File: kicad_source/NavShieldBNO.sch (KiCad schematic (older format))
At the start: 48 parts, among them CN1 ARDUINO_MKR, CN2 CONN_01X04, CN3 CONN_01X04, U1 BNO085, U2 BMP388, U3 BMP280, U4 BME280, Y1 DNI

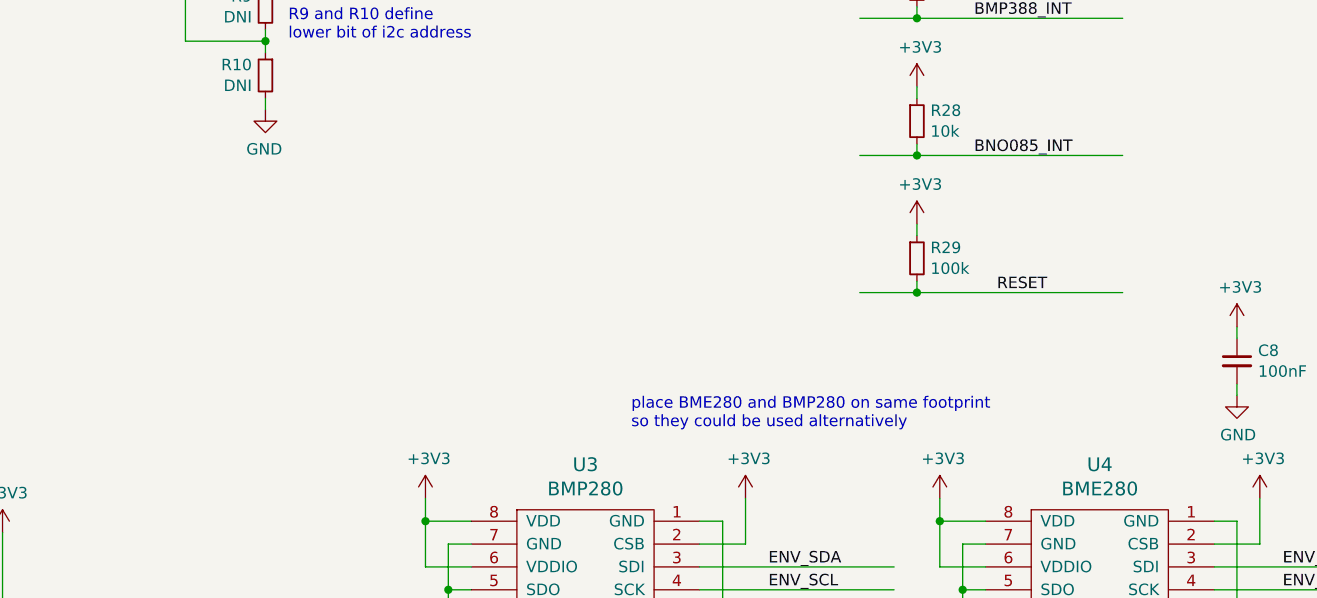
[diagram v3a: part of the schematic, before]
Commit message: added Vishay VCNL4040
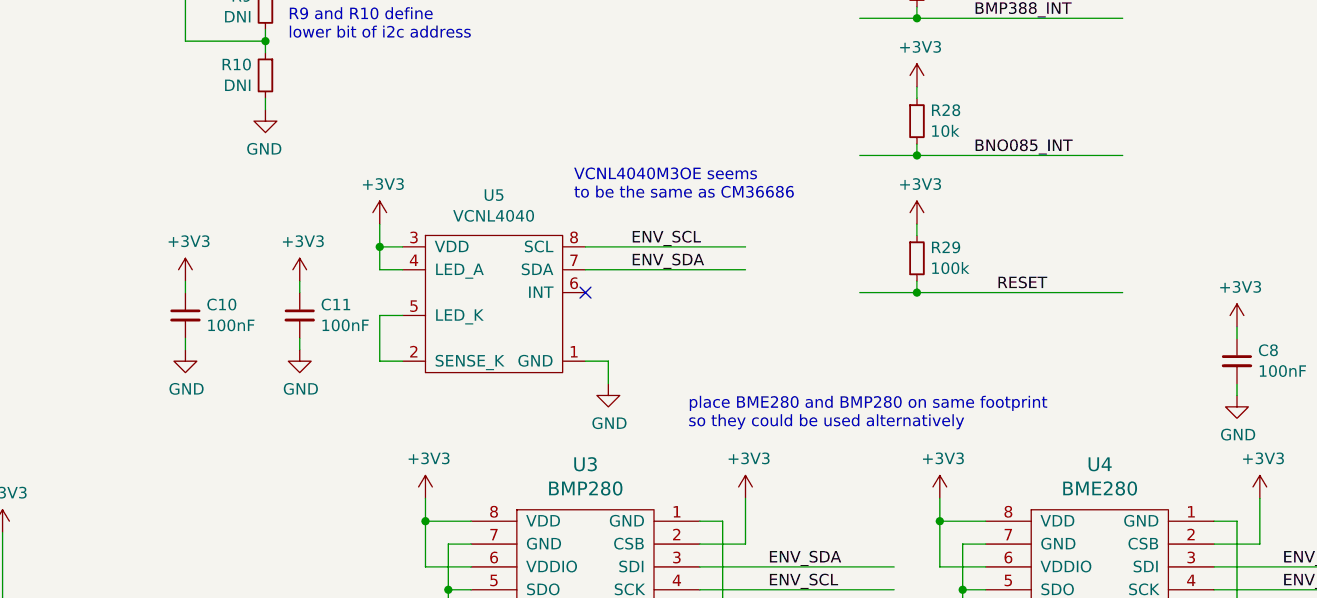
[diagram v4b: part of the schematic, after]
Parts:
- added C10, C11: 100nF, capacitors:C_0603, symbol devices:C_0603
- added U5: VCNL4040, IC_sensor:VCNL4040, symbol IC_sensor:VCNL4040
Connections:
- wire segments 210 -> 225
- no-connect marks 12 -> 13
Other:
- note added: "VCNL4040M3OE seems \nto be the same as CM36686"
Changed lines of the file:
@@
 Wire Wire Line
 	10850 5000 10850 5050
-Text Notes 7700 5450 0    50   ~ 0
+Text Notes 7950 5450 0    50   ~ 0
 place BME280 and BMP280 on same footprint\nso they could be used alternatively
+Text Notes 7450 4450 0    50   ~ 0
+VCNL4040M3OE seems \nto be the same as CM36686
+$Comp
+L IC_sensor:VCNL4040 U5
+U 1 1 5F712BB0
+P 7100 4900
+F 0 "U5" H 7100 5375 50  0000 C CNN
+F 1 "VCNL4040" H 7100 5284 50  0000 C CNN
+F 2 "IC_sensor:VCNL4040" H 7150 4750 50  0001 C CNN
+F 3 "" H 7150 4750 50  0001 C CNN
+	1    7100 4900
+	1    0    0    -1
+$EndComp
+$Comp
+L devices:C_0603 C10
+U 1 1 5F7145FC
+P 5750 4950
+F 0 "C10" H 5842 4996 50  0000 L CNN
+F 1 "100nF" H 5842 4905 50  0000 L CNN
+F 2 "capacitors:C_0603" H 5750 4800 50  0001 C CNN
+F 3 "" H 5750 4950 50  0000 C CNN
+	1    5750 4950
+	1    0    0    -1
+$EndComp
+$Comp
+L power-supply:GND #PWR050
+U 1 1 5F714606
+P 5750 5100
+F 0 "#PWR050" H 5750 4850 50  0001 C CNN
+F 1 "GND" H 5755 4927 50  0000 C CNN
+F 2 "" H 5750 5100 50  0000 C CNN
+F 3 "" H 5750 5100 50  0000 C CNN
+	1    5750 5100
+	1    0    0    -1
+$EndComp
+$Comp
+L power-supply:+3V3 #PWR049
+U 1 1 5F714610
+P 5750 4800
+F 0 "#PWR049" H 5750 4650 50  0001 C CNN
+F 1 "+3V3" H 5765 4973 50  0000 C CNN
+F 2 "" H 5750 4800 50  0000 C CNN
+F 3 "" H 5750 4800 50  0000 C CNN
+	1    5750 4800
+	1    0    0    -1
+$EndComp
+Wire Wire Line
+	5750 5050 5750 5100
+Wire Wire Line
+	5750 4800 5750 4850
+$Comp
+L devices:C_0603 C11
+U 1 1 5F71461C
+P 6250 4950
+F 0 "C11" H 6342 4996 50  0000 L CNN
+F 1 "100nF" H 6342 4905 50  0000 L CNN
+F 2 "capacitors:C_0603" H 6250 4800 50  0001 C CNN
+F 3 "" H 6250 4950 50  0000 C CNN
+	1    6250 4950
+	1    0    0    -1
+$EndComp
+$Comp
+L power-supply:GND #PWR052
+U 1 1 5F714626
+P 6250 5100
+F 0 "#PWR052" H 6250 4850 50  0001 C CNN
+F 1 "GND" H 6255 4927 50  0000 C CNN
+F 2 "" H 6250 5100 50  0000 C CNN
+F 3 "" H 6250 5100 50  0000 C CNN
+	1    6250 5100
+	1    0    0    -1
+$EndComp
+$Comp
+L power-supply:+3V3 #PWR051
+U 1 1 5F714630
+P 6250 4800
+F 0 "#PWR051" H 6250 4650 50  0001 C CNN
+F 1 "+3V3" H 6265 4973 50  0000 C CNN
+F 2 "" H 6250 4800 50  0000 C CNN
+F 3 "" H 6250 4800 50  0000 C CNN
+	1    6250 4800
+	1    0    0    -1
+$EndComp
+Wire Wire Line
+	6250 5050 6250 5100
+Wire Wire Line
+	6250 4800 6250 4850
+$Comp
+L power-supply:+3V3 #PWR053
+U 1 1 5F722D98
+P 6600 4550
+F 0 "#PWR053" H 6600 4400 50  0001 C CNN
+F 1 "+3V3" H 6615 4723 50  0000 C CNN
+F 2 "" H 6600 4550 50  0000 C CNN
+F 3 "" H 6600 4550 50  0000 C CNN
+	1    6600 4550
+	1    0    0    -1
+$EndComp
+$Comp
+L power-supply:GND #PWR054
+U 1 1 5F723279
+P 7600 5250
+F 0 "#PWR054" H 7600 5000 50  0001 C CNN
+F 1 "GND" H 7605 5077 50  0000 C CNN
+F 2 "" H 7600 5250 50  0000 C CNN
+F 3 "" H 7600 5250 50  0000 C CNN
+	1    7600 5250
+	1    0    0    -1
+$EndComp
+Wire Wire Line
+	8200 4650 7500 4650
+Wire Wire Line
+	8200 4750 7500 4750
+Wire Wire Line
+	7500 5150 7600 5150
+Wire Wire Line
+	7600 5150 7600 5250
+Wire Wire Line
+	6700 5150 6600 5150
+Wire Wire Line
+	6600 5150 6600 4950
+Wire Wire Line
+	6600 4950 6700 4950
+Wire Wire Line
+	6700 4750 6600 4750
+Wire Wire Line
+	6600 4750 6600 4650
+Wire Wire Line
+	6700 4650 6600 4650
+Connection ~ 6600 4650
+Wire Wire Line
+	6600 4650 6600 4550
+Text Label 7700 4750 0    50   ~ 0
+ENV_SDA
+Text Label 7700 4650 0    50   ~ 0
+ENV_SCL
+NoConn ~ 7500 4850
 $EndSCHEMATC

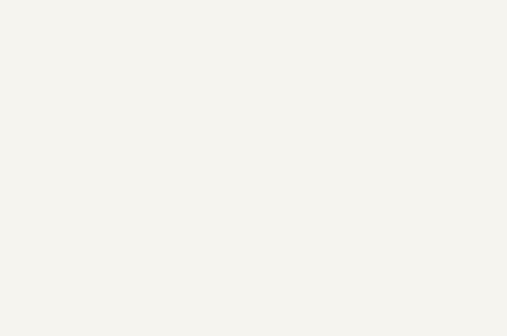
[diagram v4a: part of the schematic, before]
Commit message: added logo, updated images and pdf
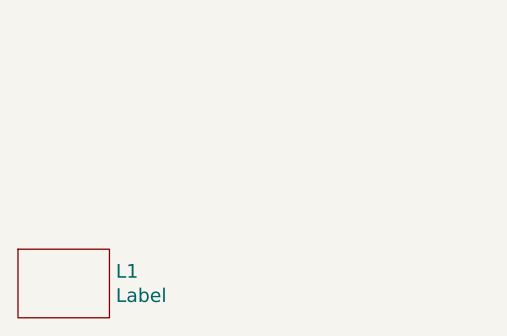
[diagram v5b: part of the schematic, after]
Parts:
- added L1: Label, labels:generationmake_small_solder, symbol devices:Label
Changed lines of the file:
@@
 Sheet 1 1
 Title "NavShieldBNO"
-Date "2020-09-25"
-Rev "dev_0.1"
+Date "2020-09-27"
+Rev "0.1"
 Comp "generationmake"
 Comment1 ""
@@
 ENV_SCL
 NoConn ~ 7500 4850
+$Comp
+L devices:Label L1
+U 1 1 5F79EEB6
+P 700 7600
+F 0 "L1" H 928 7653 60  0000 L CNN
+F 1 "Label" H 928 7547 60  0000 L CNN
+F 2 "labels:generationmake_small_solder" H 600 7700 60  0001 C CNN
+F 3 "" H 700 7600 60  0000 C CNN
+	1    700  7600
+	1    0    0    -1
+$EndComp
 $EndSCHEMATC

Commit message: updated layout, made DRC, updated silk screen
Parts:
- added L2: Label, labels:generationmake_logo, symbol devices:Label
- added W1, W2, W3, W4, W5, W6, W7, W8: TEST_1P, wire_pads:SolderWirePad_single_1mmSMD, symbol mechanical-connectors:TEST_1P
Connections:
- net labels added: INT
- wire segments 225 -> 231
- no-connect marks 13 -> 12
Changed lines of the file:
@@
 Text Label 7700 4650 0    50   ~ 0
 ENV_SCL
-NoConn ~ 7500 4850
 $Comp
 L devices:Label L1
@@
 	1    0    0    -1
 $EndComp
+$Comp
+L mechanical-connectors:TEST_1P W3
+U 1 1 5F71EF96
+P 5800 6700
+F 0 "W3" V 5750 6650 50  0000 L CNN
+F 1 "TEST_1P" V 5845 6888 50  0000 L CNN
+F 2 "wire_pads:SolderWirePad_single_1mmSMD" H 6000 6700 50  0001 C CNN
+F 3 "" H 6000 6700 50  0000 C CNN
+	1    5800 6700
+	0    1    1    0
+$EndComp
+$Comp
+L mechanical-connectors:TEST_1P W4
+U 1 1 5F71FCBA
+P 5800 6800
+F 0 "W4" V 5750 6750 50  0000 L CNN
+F 1 "TEST_1P" V 5845 6988 50  0000 L CNN
+F 2 "wire_pads:SolderWirePad_single_1mmSMD" H 6000 6800 50  0001 C CNN
+F 3 "" H 6000 6800 50  0000 C CNN
+	1    5800 6800
+	0    1    1    0
+$EndComp
+$Comp
+L mechanical-connectors:TEST_1P W5
+U 1 1 5F71FE99
+P 5800 6900
+F 0 "W5" V 5750 6850 50  0000 L CNN
+F 1 "TEST_1P" V 5845 7088 50  0000 L CNN
+F 2 "wire_pads:SolderWirePad_single_1mmSMD" H 6000 6900 50  0001 C CNN
+F 3 "" H 6000 6900 50  0000 C CNN
+	1    5800 6900
+	0    1    1    0
+$EndComp
+$Comp
+L mechanical-connectors:TEST_1P W6
+U 1 1 5F720010
+P 5800 7000
+F 0 "W6" V 5750 6950 50  0000 L CNN
+F 1 "TEST_1P" V 5845 7188 50  0000 L CNN
+F 2 "wire_pads:SolderWirePad_single_1mmSMD" H 6000 7000 50  0001 C CNN
+F 3 "" H 6000 7000 50  0000 C CNN
+	1    5800 7000
+	0    1    1    0
+$EndComp
+$Comp
+L mechanical-connectors:TEST_1P W7
+U 1 1 5F72016B
+P 5800 7100
+F 0 "W7" V 5750 7050 50  0000 L CNN
+F 1 "TEST_1P" V 5845 7288 50  0000 L CNN
+F 2 "wire_pads:SolderWirePad_single_1mmSMD" H 6000 7100 50  0001 C CNN
+F 3 "" H 6000 7100 50  0000 C CNN
+	1    5800 7100
+	0    1    1    0
+$EndComp
+$Comp
+L mechanical-connectors:TEST_1P W1
+U 1 1 5F72032F
+P 2000 3450
+F 0 "W1" V 1954 3638 50  0000 L CNN
+F 1 "TEST_1P" V 2045 3638 50  0000 L CNN
+F 2 "wire_pads:SolderWirePad_single_1mmSMD" H 2200 3450 50  0001 C CNN
+F 3 "" H 2200 3450 50  0000 C CNN
+	1    2000 3450
+	0    1    1    0
+$EndComp
+$Comp
+L mechanical-connectors:TEST_1P W2
+U 1 1 5F722ECE
+P 2000 3650
+F 0 "W2" V 1954 3838 50  0000 L CNN
+F 1 "TEST_1P" V 2045 3838 50  0000 L CNN
+F 2 "wire_pads:SolderWirePad_single_1mmSMD" H 2200 3650 50  0001 C CNN
+F 3 "" H 2200 3650 50  0000 C CNN
+	1    2000 3650
+	0    1    1    0
+$EndComp
+Wire Wire Line
+	2000 3450 1850 3450
+Connection ~ 1850 3450
+Wire Wire Line
+	2000 3650 1950 3650
+Wire Wire Line
+	1950 3650 1950 3550
+Connection ~ 1950 3550
+$Comp
+L mechanical-connectors:TEST_1P W8
+U 1 1 5F7687A2
+P 8000 4950
+F 0 "W8" V 7954 5138 50  0000 L CNN
+F 1 "TEST_1P" V 8045 5138 50  0000 L CNN
+F 2 "wire_pads:SolderWirePad_single_1mmSMD" H 8200 4950 50  0001 C CNN
+F 3 "" H 8200 4950 50  0000 C CNN
+	1    8000 4950
+	0    1    1    0
+$EndComp
+Wire Wire Line
+	7500 4850 7600 4850
+Wire Wire Line
+	7600 4850 7600 4950
+Wire Wire Line
+	7600 4950 8000 4950
+Text Label 7650 4950 0    50   ~ 0
+INT
+$Comp
+L devices:Label L2
+U 1 1 5F77DB51
+P 1400 7600
+F 0 "L2" H 1628 7653 60  0000 L CNN
+F 1 "Label" H 1628 7547 60  0000 L CNN
+F 2 "labels:generationmake_logo" H 1300 7700 60  0001 C CNN
+F 3 "" H 1400 7600 60  0000 C CNN
+	1    1400 7600
+	1    0    0    -1
+$EndComp
